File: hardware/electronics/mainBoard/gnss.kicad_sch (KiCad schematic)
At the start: 19 parts, among them J2 Bus_M.2_Socket_E, J4 M.2 Standoff, U6 TXS0104VxRUTR, U8 TPS22996H-Q1

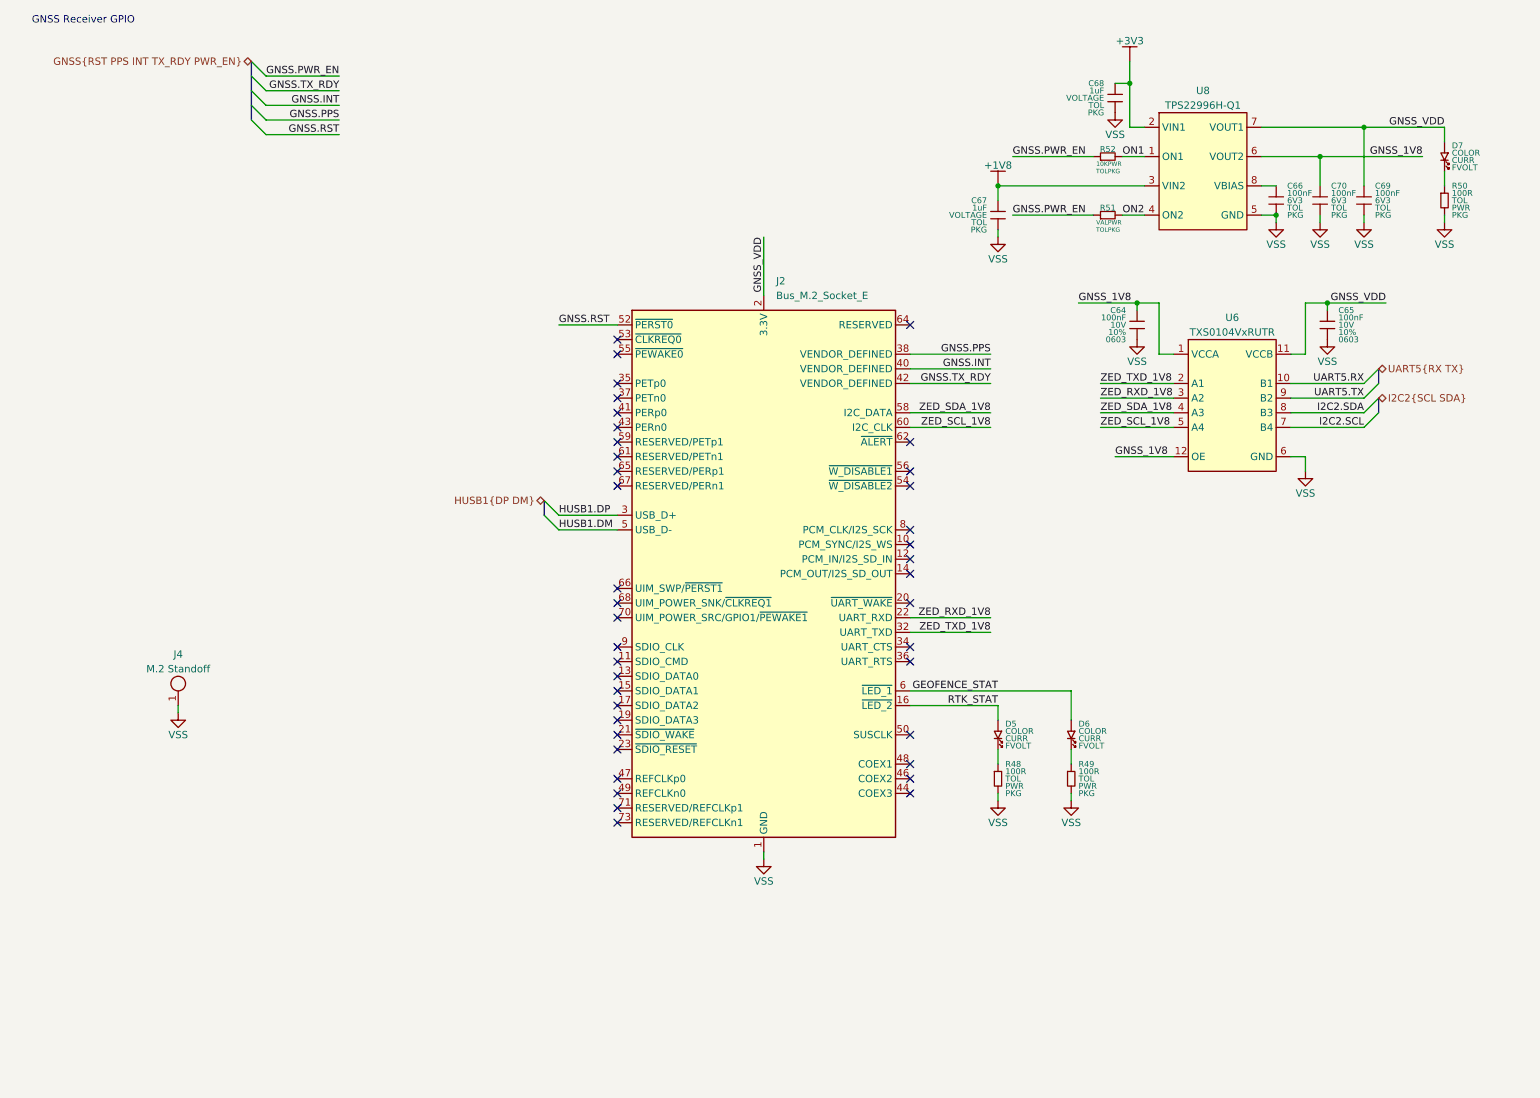
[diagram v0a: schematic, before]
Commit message: added signal level switch for level shifter
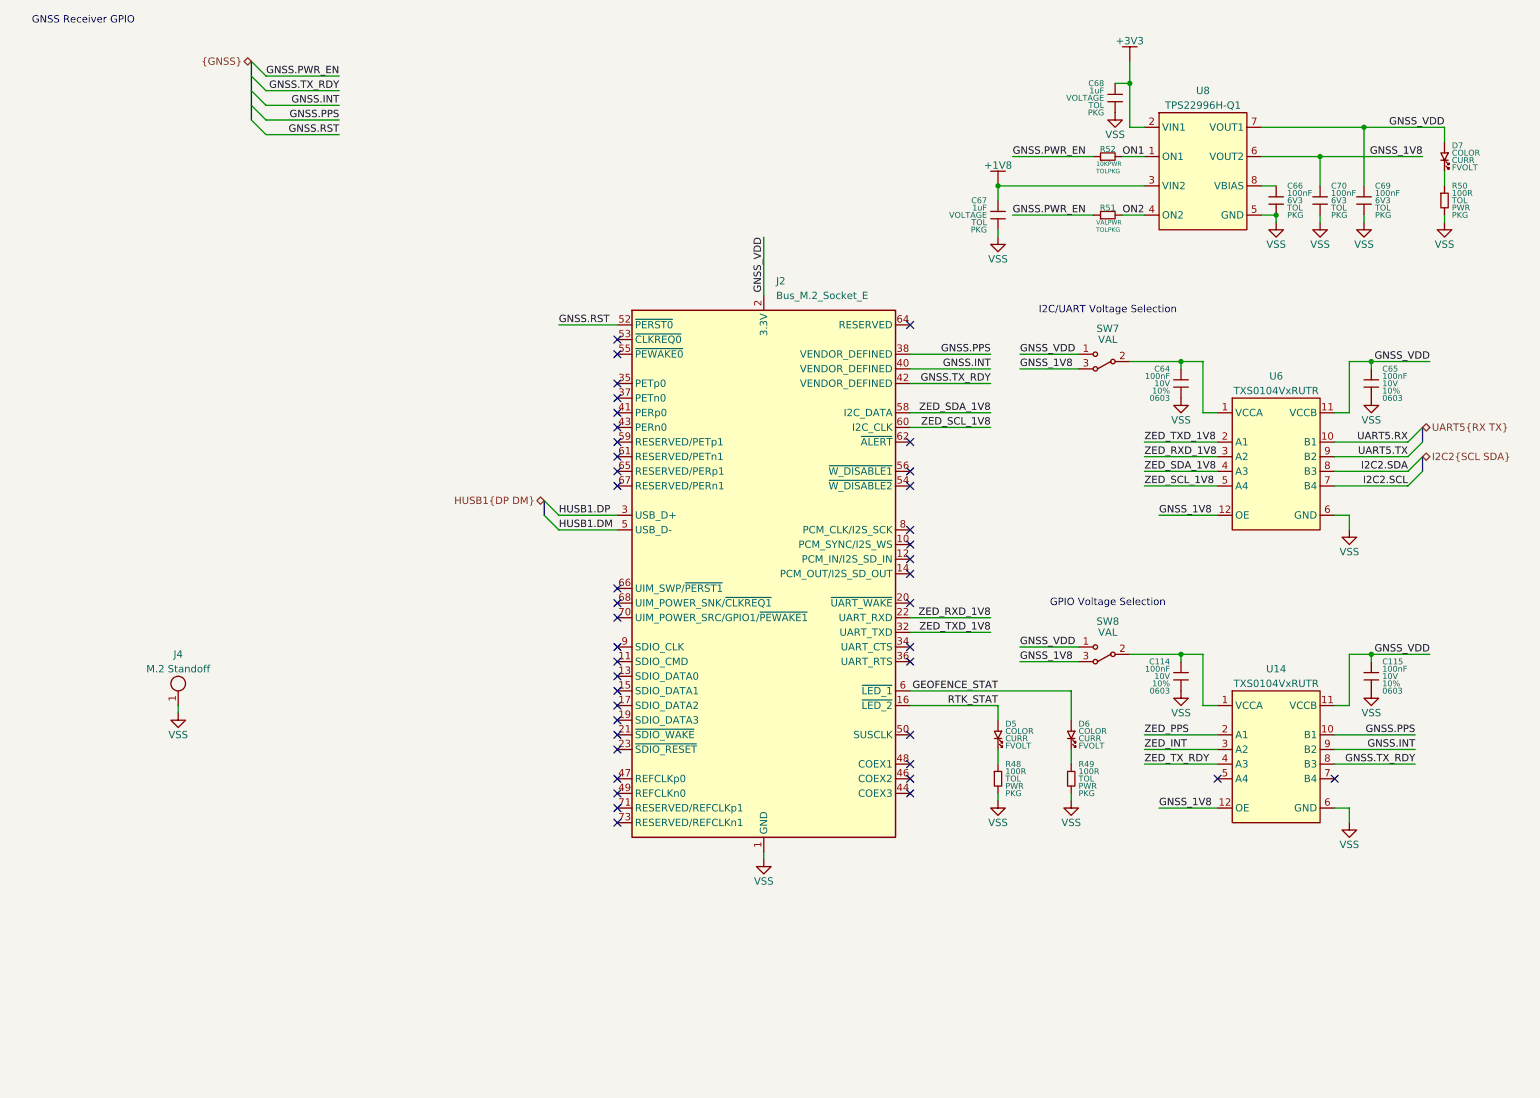
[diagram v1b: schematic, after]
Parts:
- added C114, C115: 100nF, lib_fp:MLCC0603, symbol lib_sch:C
- added SW7, SW8: VAL, symbol .DS-Switches:SPDT
- added U14: TXS0104VxRUTR, lib_fp:RUT0012A, symbol lib_sch:TXS0104VxRUTR
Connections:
- net GNSS.INT: now also U14.9 (B2)
- net GNSS.PPS: now also U14.10 (B1)
- net GNSS.TX_RDY: now also U14.8 (B3)
- net GNSS_1V8: now also SW7.3, SW8.3, U14.12 (OE); no longer C64.1, U6.1 (VCCA)
- net GNSS_VDD: now also C115.1, SW7.1, SW8.1, U14.11 (VCCB)
- net VSS: now also C114.2, C115.2, U14.6 (GND)
- new net: C64.1, SW7.2, U6.1 (VCCA)
- new net: C114.1, SW8.2, U14.1 (VCCA)
- new net ZED_INT: U14.3 (A2)
- new net ZED_PPS: U14.2 (A1)
- new net ZED_TX_RDY: U14.4 (A3)
- no-connect marks 40 -> 42
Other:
- note added: "GPIO Voltage Selection"
- note added: "I2C/UART Voltage Selection"
- moved on the sheet: C64, C65, U6

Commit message: added hw for GNSS card
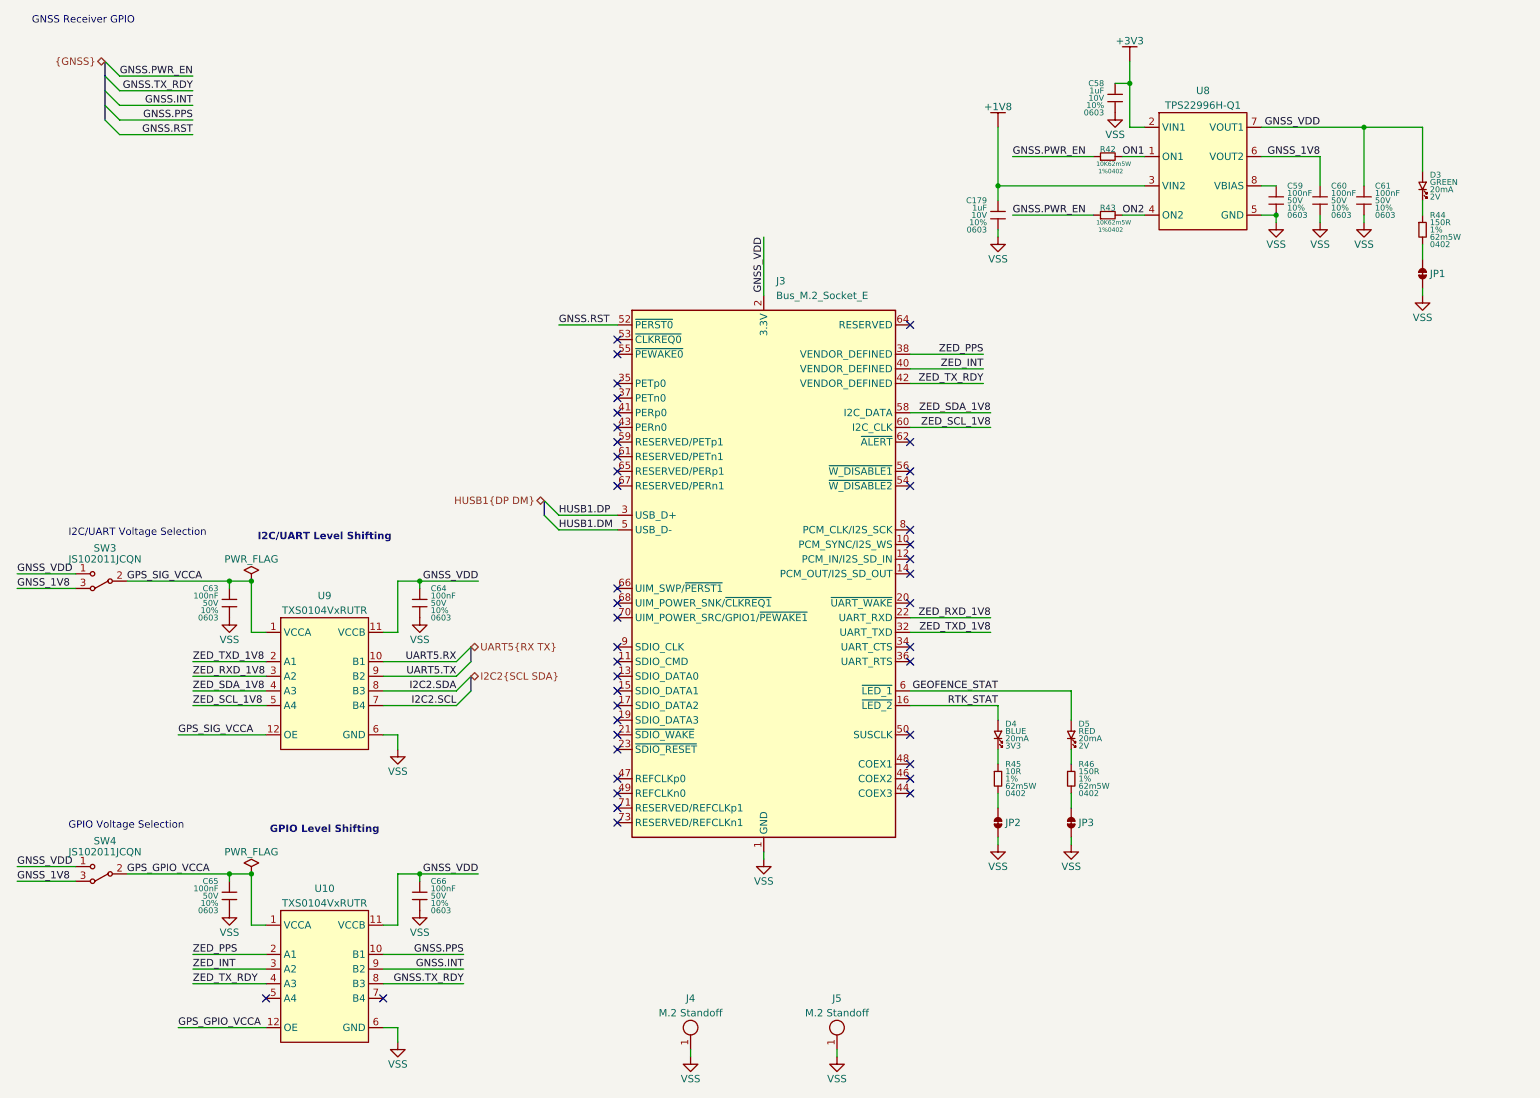
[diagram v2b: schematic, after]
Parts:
- removed C114, C115: 100nF, lib_fp:MLCC0603, symbol lib_sch:C
- removed C67, C68: 1uF, symbol lib_sch:C
- removed C69, C70: 100nF, symbol lib_sch:C
- removed D7: ~, symbol lib_sch:LED
- removed R48, R49, R50: 100R, symbol lib_sch:R
- removed R51: VAL, symbol lib_sch:R_horizontal
- removed R52: 10K, symbol lib_sch:R_horizontal
- removed SW8: VAL, symbol .DS-Switches:SPDT
- added C179, C58: 1uF, symbol lib_sch:C
- added C59, C60, C61, C63: 100nF, symbol lib_sch:C
- added D3: LTST-C191KGKT, symbol lib_sch:LED
- added J5: M.2 Standoff, symbol lib_sch:Mounting-Hole
- added JP1, JP2, JP3: ~, symbol lib_sch:Jumper_2_Bridged
- added R42, R43: 10K, symbol lib_sch:R_horizontal
- added R44, R46: 150R, symbol lib_sch:R
- added R45: 10R, symbol lib_sch:R
- added SW4: JS102011JCQN, symbol lib_sch:SPDT
- C64, C65: footprint lib_fp:MLCC0603 -> (none); DKPN 478-KAM15AR71A104KTCT-ND -> 478-KAM15AR71H104KTCT-ND; MPN KAM15AR71A104KT -> 06035C104K4T2A; Voltage Rating 10V -> 50V
- C66: DKPN (none) -> 478-KAM15AR71H104KTCT-ND; MPN (none) -> 06035C104K4T2A; Manufacturer (none) -> KYOCERA AVX; Package PKG -> 0603; Tolerance TOL -> 10%; Voltage Rating 6V3 -> 50V
- D4: renamed from D5; value ~ -> LTST-C191TBKT; Color COLOR -> BLUE; Current CURR -> 20mA; DKPN (none) -> 160-1647-1-ND; Forward Voltage FVOLT -> 3V3; MPN (none) -> LTST-C191TBKT; Manufacturer (none) -> Lite-On Inc.
- D5: renamed from D6; value ~ -> LTST-C191KRKT; Color COLOR -> RED; Current CURR -> 20mA; DKPN (none) -> 160-1447-1-ND; Forward Voltage FVOLT -> 2V; MPN (none) -> LTST-C191KRKT; Manufacturer (none) -> Lite-On Inc.
- J3: renamed from J2; DKPN (none) -> MDT420E01001CT-ND; MPN (none) -> MDT420E01001; Manufacturer (none) -> Amphenol ICC (FCI)
- J4: DKPN (none) -> 4827-123A-NUT-42CT-ND; MPN (none) -> 123A-NUT-42; Manufacturer (none) -> ATTEND Technology
- SW3: renamed from SW7; value VAL -> JS102011JCQN; symbol .DS-Switches:SPDT -> lib_sch:SPDT; DKPN (none) -> CKN10721CT-ND; MPN (none) -> C&K; Manufacturer (none) -> JS102011JCQN
- U10: renamed from U14; footprint lib_fp:RUT0012A -> (none)
- U9: renamed from U6; footprint lib_fp:RUT0012A -> (none)
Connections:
- net +1V8: now also C179.1
- net +3V3: now also C58.1
- net GNSS.INT: no longer J3.40 (VENDOR_DEFINED)
- net GNSS.PPS: no longer J3.38 (VENDOR_DEFINED)
- net GNSS.PWR_EN: now also R42.1, R43.1
- net GNSS.TX_RDY: no longer J3.42 (VENDOR_DEFINED)
- net GNSS_1V8: now also C60.1, SW4.3; no longer U10.12 (OE), U9.12 (OE)
- net GNSS_VDD: now also C64.1, C66.1, C61.1, D3.1, SW4.1; no longer C65.1
- net ON1: now also R42.2
- net ON2: now also R43.2
- net VSS: now also C179.2, C58.2, C59.2, C60.2, C61.2, C63.2, J5.1, JP1.2, JP2.2, JP3.2
- net ZED_INT: now also J3.40 (VENDOR_DEFINED)
- net ZED_PPS: now also J3.38 (VENDOR_DEFINED)
- net ZED_TX_RDY: now also J3.42 (VENDOR_DEFINED)
- net at D5.2: now also R46.1
- net at U8.8 (VBIAS): now also C59.1; no longer C66.1
- net GPS_SIG_VCCA: now reaches SW3.2, U9.1 (VCCA)
- net GPS_SIG_VCCA: now also U9.12 (OE), C63.1; no longer C64.1
- net at D4.2: now also R45.1
- net GPS_GPIO_VCCA: now reaches U10.1 (VCCA)
- net GPS_GPIO_VCCA: now also C65.1, U10.12 (OE), SW4.2
- new net: JP2.1, R45.2
- new net: JP3.1, R46.2
- new net: D3.2, R44.1
- new net: JP1.1, R44.2
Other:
- note added: "GPIO Level Shifting"
- note added: "I2C/UART Level Shifting"
- moved on the sheet: J4, SW3, U10, U9

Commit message: fixed power flags
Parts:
- renumbered C58 to C44, C59 to C45, C60 to C46, C61 to C47, C179 to C48, C63 to C49, C64 to C50, C65 to C51, C66 to C52, R42 to R33, R43 to R34, R44 to R35, R45 to R36, R46 to R37, U8 to U7, U9 to U8, U10 to U9
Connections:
- net HUSB1.DM: no longer names the net of J3.5 (USB_D-)
- net HUSB1.DP: no longer names the net of J3.3 (USB_D+)
- no-connect marks 42 -> 44

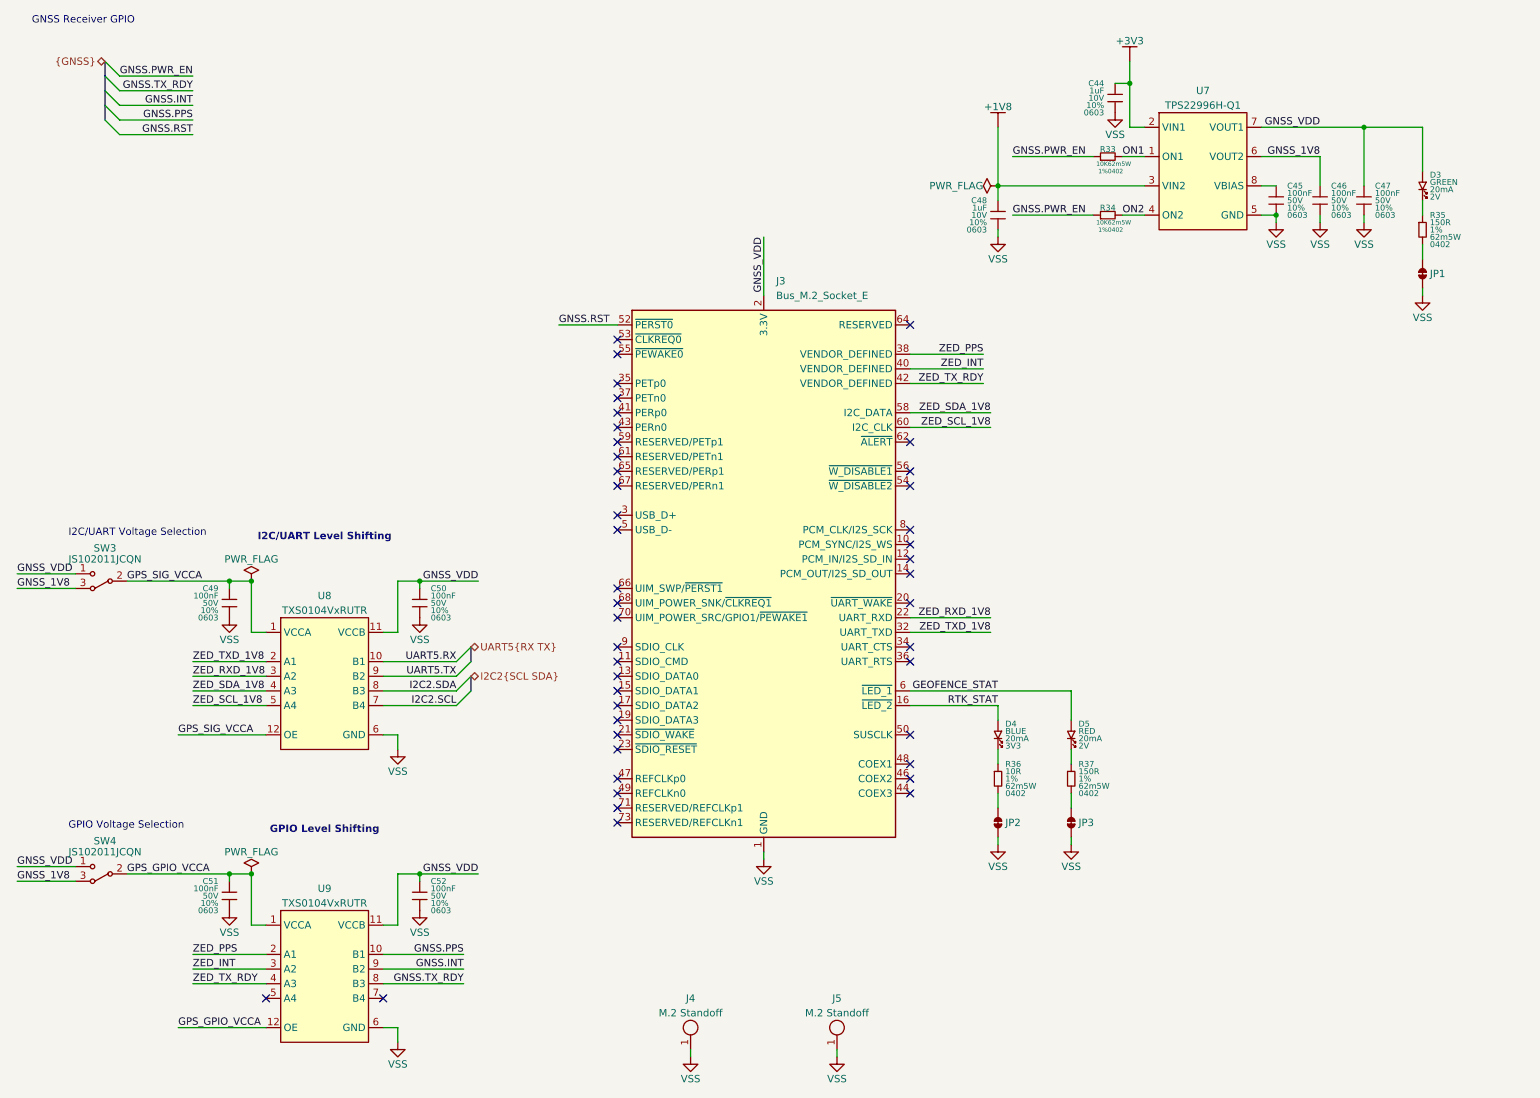
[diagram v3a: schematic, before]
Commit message: updated capacitors
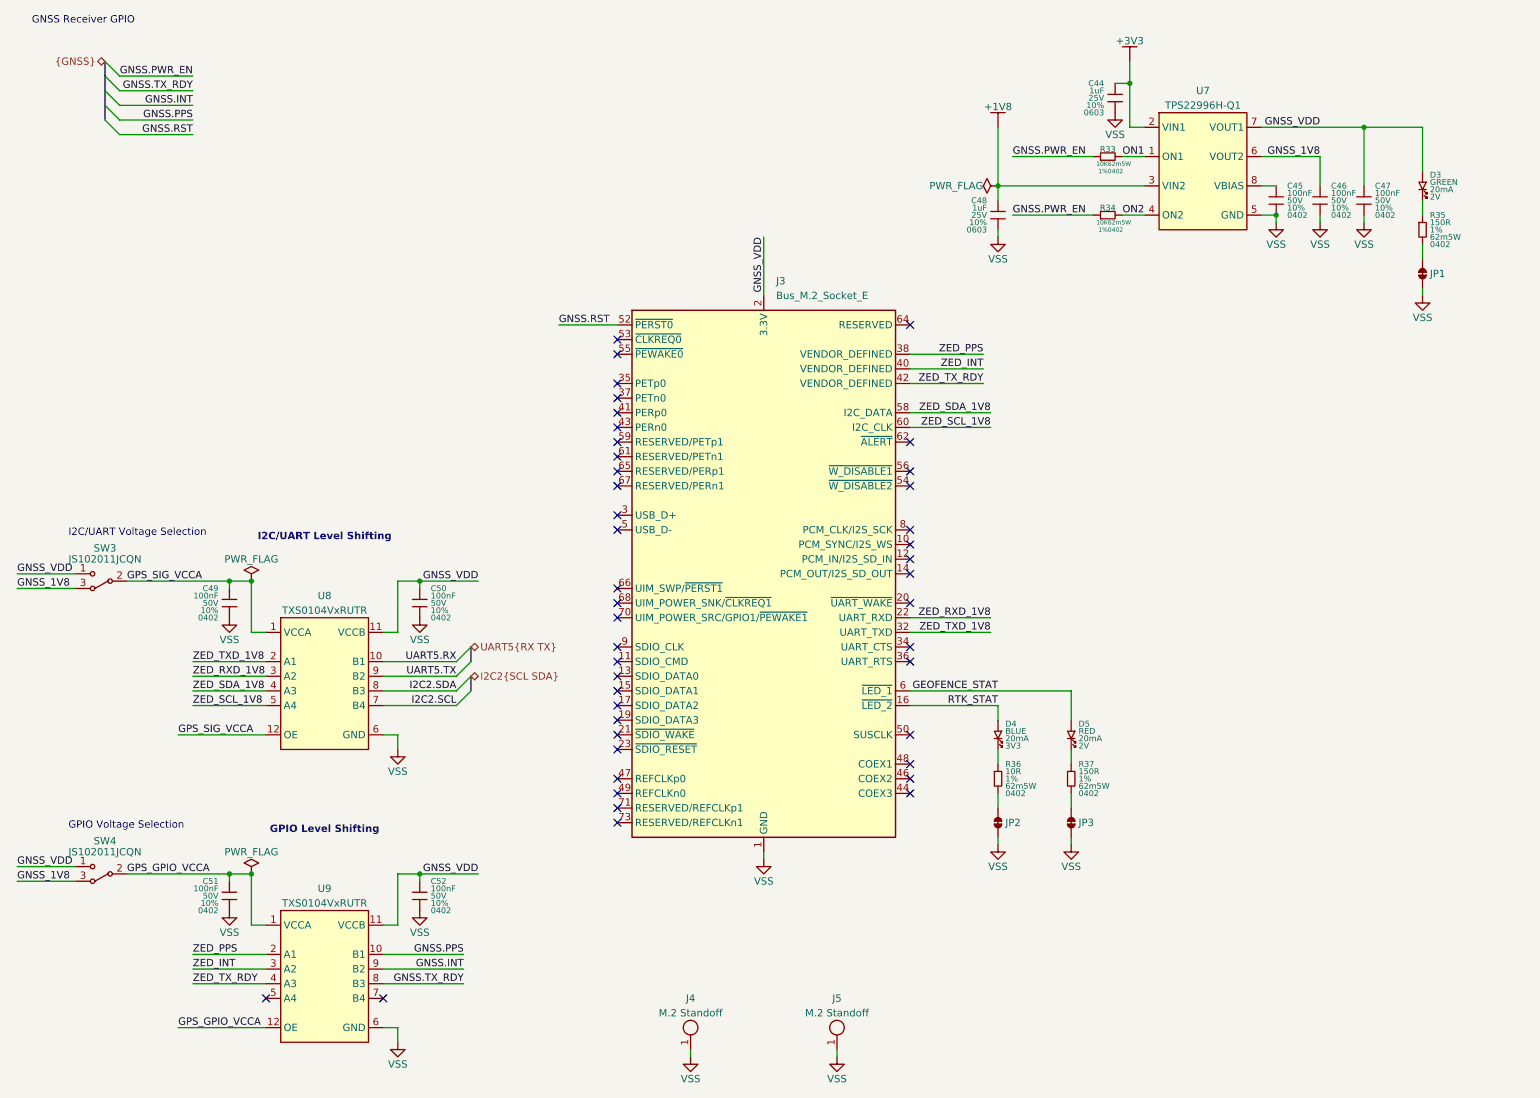
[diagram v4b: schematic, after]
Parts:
- C44, C48: DKPN 478-KAM15AR71A105KTCT-ND -> 490-GRT188R71E105KE13DCT-ND; MPN KAM15AR71A105KT -> GRT188R71E105KE13D; Manufacturer KYOCERA AVX -> Murata Electronics; Voltage Rating 10V -> 25V
- C45, C46, C47, C49, C50, C51, C52: DKPN 478-KAM15AR71H104KTCT-ND -> 490-GRT155R71H104KE01DCT-ND; MPN 06035C104K4T2A -> GRT155R71H104KE01D; Manufacturer KYOCERA AVX -> Murata Electronics; Package 0603 -> 0402
